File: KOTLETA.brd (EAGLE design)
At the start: 27 x 40.2 mm, 107 parts, among them CON1 SM06B-SRSS-TB, CON2 CON-4P-JST_GH-RA, CON3 CON-4P-JST_GH-RA, IC1 STM32F105RCT6, IC2 CAT24C02, IC3 SN65HVD232D, IC4 LMR14010ADDCT, IC5 LM75BD-TSSOP8, IC6 FAN7888, IC7 ZXCT1051, IC8 3.3V, Q1 CSD18510Q5B, Q2 CSD18510Q5B, Q3 CSD18510Q5B, Q4 CSD18510Q5B, Q5 CSD18510Q5B, Q6 CSD18510Q5B, X1 24MHz

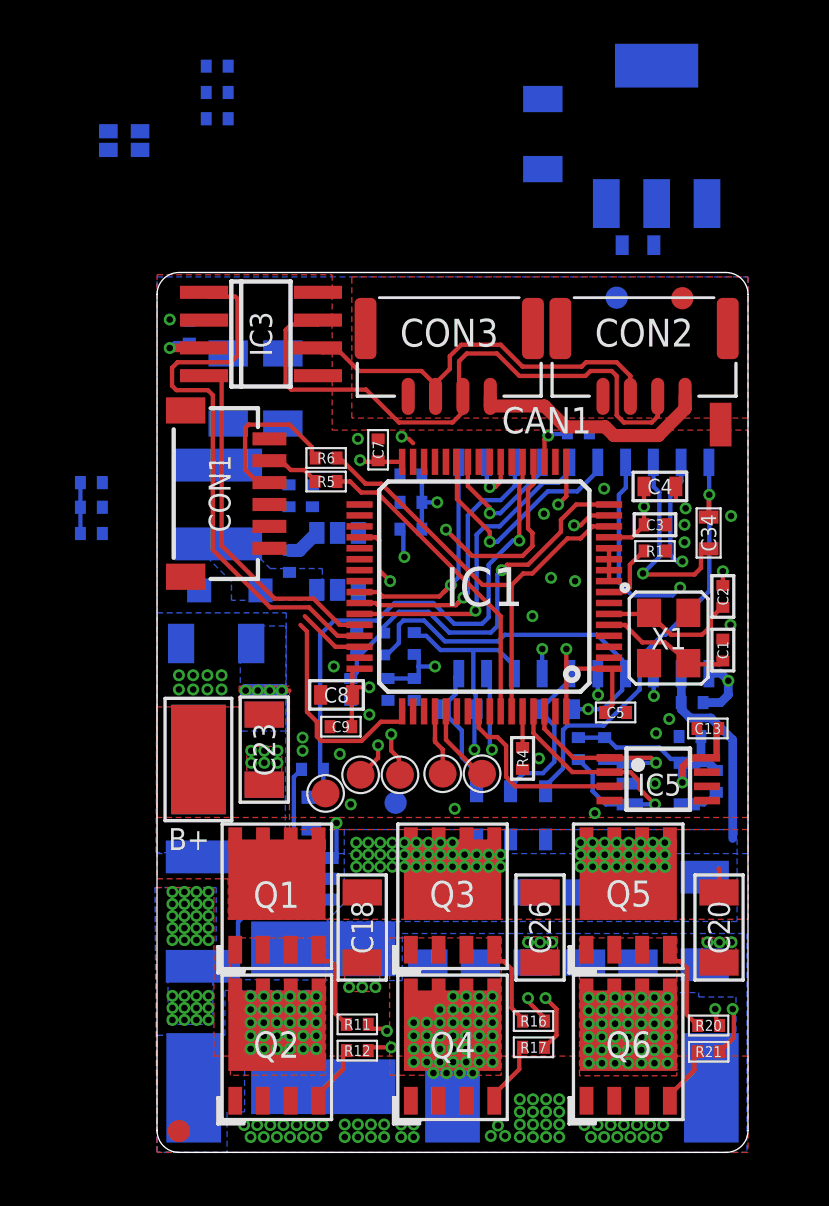
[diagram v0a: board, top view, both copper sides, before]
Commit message: proper gitignore
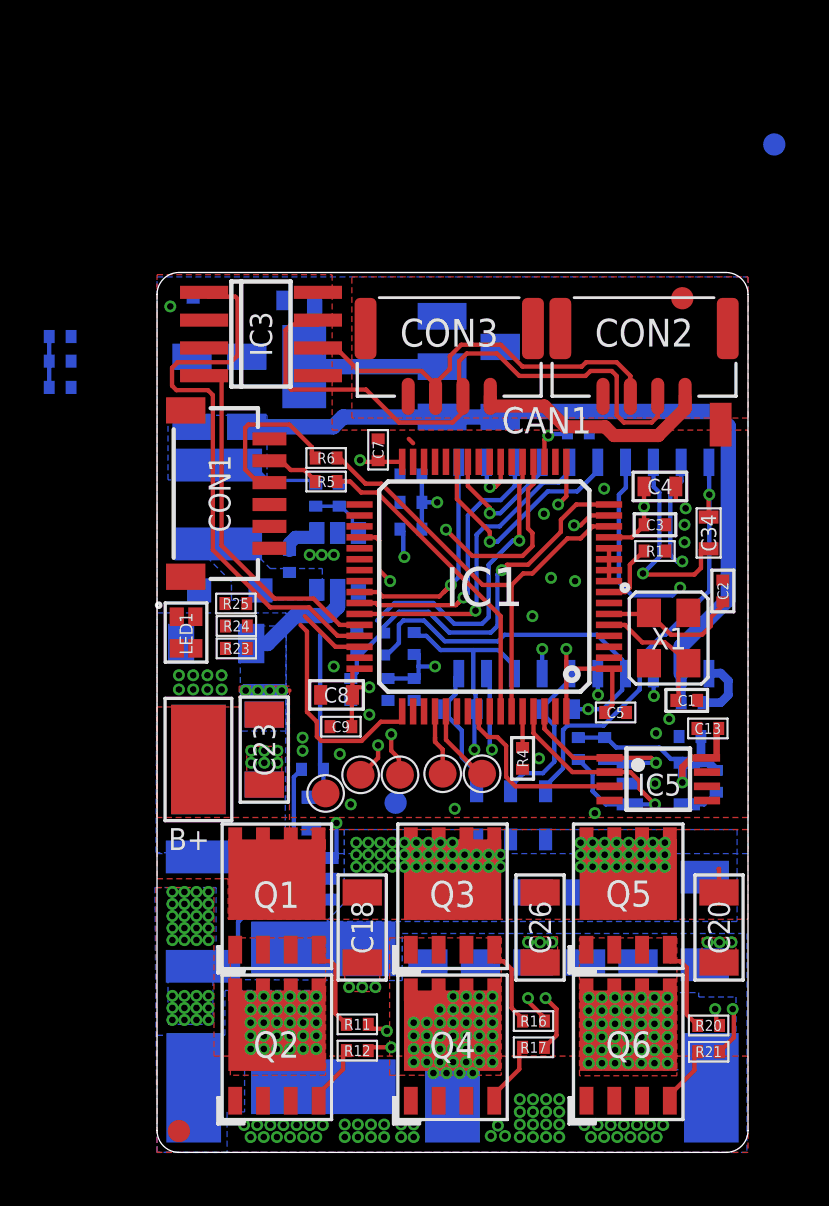
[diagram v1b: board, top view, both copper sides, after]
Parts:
- moved R25 24.6 mm to (3.60, 25.1), flipped to the top
- moved R24 24.4 mm to (3.62, 24.1), flipped to the top
- moved R23 24.2 mm to (3.62, 23.0), flipped to the top
- moved LED1 22.7 mm to (1.32, 23.8), flipped to the top, turned to 0 degrees
- moved IC8 16.7 mm to (9.88, 35.9), turned to 270 degrees
- moved C29 15.7 mm to (6.47, 38.9)
- moved C27 11.5 mm to (15.7, 35.2)
- moved FD3 10.0 mm to (28.2, 46.0)
- moved R9 6.83 mm to (-4.42, 35.0)
- moved C15 6.83 mm to (-4.42, 37.3)
- moved R8 6.83 mm to (-4.42, 36.1)
- moved C1 2.83 mm to (24.2, 20.6), turned to 180 degrees
- moved C36 1.66 mm to (4.10, 34.8)
- moved C38 1.66 mm to (1.60, 34.8)
- moved R27 1.23 mm to (7.25, 30.0)
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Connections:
- net VBAT: no longer C14.1, IC6.12
- net VDD_9V: now also C14.1, IC6.12
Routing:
- net VDD_9V: track 0.72 -> 40.9 mm
- net VDD_3V3: track 40.4 -> 47.4 mm, vias 9 -> 8
- net VBAT: track 14.4 -> 10.7 mm
- net SENSE_CURRENT: track 24.7 -> 21.8 mm
- net N$24: track 0.00 -> 2.71 mm
- net GND: track 8.41 -> 7.76 mm, vias 41 -> 38
- net N$7: track 0.64 -> 0.00 mm
- added copper zone on layer 16, net VDD_9V

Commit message: routing done
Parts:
- R14: value 0.005 OHM -> 0.005R; device sapog_reference_hardware:2010_CURRENT_SHUNT -> SHUNT_RESISTORS:R2010-KELVIN
- X1: device GNSS2_master_lib:OSCILLATOR-3.2X2.5 -> crystal:OSCILLATOR-3.2X2.5-4P
- moved C28 19.4 mm to (15.7, 32.9), flipped to the top, turned to 0 degrees
- moved C15 16.3 mm to (10.2, 30.1), turned to 90 degrees
- moved R9 14.5 mm to (9.22, 30.1), turned to 270 degrees
- moved R8 13.9 mm to (8.72, 31.6), turned to 0 degrees
- moved R7 9.10 mm to (11.8, 25.3)
- moved FD3 7.32 mm to (25.6, 39.2)
- moved C29 2.52 mm to (4.15, 38.0)
- moved C9 1.80 mm to (8.40, 21.2)
- moved C7 1.39 mm to (11.2, 33.0), turned to 180 degrees
- moved C8 1.30 mm to (8.80, 19.8)
- moved C30 1.06 mm to (9.90, 21.3)
- moved TP3 0.89 mm to (7.42, 17.2)
- moved R18 0.78 mm to (11.1, 23.2), turned to 270 degrees
- moved CON2 0.70 mm to (22.2, 38.1)
- moved CON3 0.70 mm to (13.3, 38.1)
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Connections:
- removed net N$15: IC7.4, R14.SENSE1
- new net N$20: IC7.4, R14.S1
- net CURRENT_SHUNT: now also R14.1, R14.11; no longer R14.CURRENT1
- net GND: now also R14.2, R14.22; no longer R14.CURRENT2
- net GNDD: no longer IC3.5
- net N$13: now also R14.S2; no longer R14.SENSE2
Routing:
- net N$12: track 0.00 -> 13.6 mm, vias 0 -> 2
- net SWDIO: track 3.08 -> 16.4 mm, vias 0 -> 2
- net SWCLK: track 10.2 -> 22.8 mm, vias 0 -> 2
- net BLABLA: track 7.08 -> 17.5 mm
- net N$3: track 0.00 -> 10.2 mm, vias 0 -> 2
- net N$18: track 0.00 -> 9.53 mm, vias 0 -> 2
- net SENSE_CURRENT: track 21.8 -> 12.7 mm
- net GNDD: track 0.59 -> 7.85 mm, vias 0 -> 2
- net VDD_3V3: track 47.4 -> 54.0 mm, vias 8 -> 15
- net SENSE_VIN: track 11.0 -> 16.1 mm
- net N$20: track 0.00 -> 5.04 mm
- net VDD_9V: track 40.9 -> 44.7 mm
- net VBAT: track 10.7 -> 14.5 mm
- net N$15: track 3.20 -> 0.00 mm
- net N$25: track 19.5 -> 22.4 mm
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- added copper zone on layer 16, net VDD_3V3
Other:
- board text removed: "CAN1"

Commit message: updates
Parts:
- CON1: value SM06B-SRSS-TB -> CON-6P; device sapog_reference_hardware:SM06B -> Connectors:SM06B
- IC2: device sapog_reference_hardware:SOT23-5L -> misc:SOT23-5L
- IC5: device sapog_reference_hardware:TSSOP8 -> misc:TSSOP8
- IC8: device sapog_reference_hardware:SOT-223 -> linear regulators:SOT-223
- LED1: device sapog_reference_hardware:LITE_ON_RGB_LED -> myxa_masterlib:LITE_ON_RGB_LED
- moved R2 0.12 mm to (20.3, 18.4)

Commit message: Updates
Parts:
- removed R28: (no value), rc:R0402
- removed U$1: (no value), sapog_reference_hardware:REF_BOARD_OUTLINE
- added PAD1, PAD10, PAD11, PAD12, PAD13, PAD14, PAD15, PAD16, PAD17, PAD18, PAD19, PAD2, PAD3, PAD4, PAD5, PAD6, PAD7, PAD8, PAD9: PAD-HOLE-0.6, PADS:HOLE_0.6
- added R29: 200R, R_digikey:R0402
- added R30: 10K, R_digikey:R0402
- R27: value (none) -> 130K
- moved FD2 24.8 mm to (25.8, 2.05)
- moved FD1 12.0 mm to (11.7, 39.1)
- moved FD3 1.10 mm to (25.7, 38.1)
- moved B+ 0.08 mm to (1.97, 17.9)
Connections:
- new net N$15: IC1.9, R29.1
- net FET_A_VS: now also PAD17.P$1, PAD7.P$1, PAD8.P$1
- net FET_B_VS: now also PAD10.P$1, PAD18.P$1, PAD9.P$1
- net FET_C_VS: now also PAD11.P$1, PAD12.P$1, PAD19.P$1
- net GND: now also PAD4.P$1, PAD5.P$1, PAD6.P$1, R30.1; no longer IC1.9, R28.1
- net GNDD: now also PAD13.P$1
- net N$22: now also PAD16.P$1
- net N$23: now also PAD15.P$1
- net N$24: now also R30.2; no longer R28.2
- net N$25: now also PAD14.P$1
- net VBAT: now also PAD1.P$1, PAD2.P$1, PAD3.P$1
- net VDD_3V3: now also R29.2
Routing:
- net N$15: track 0.00 -> 8.87 mm, vias 0 -> 1
- net N$22: track 11.1 -> 16.4 mm
- net N$23: track 27.7 -> 33.0 mm
- net GNDD: track 7.85 -> 3.25 mm, vias 2 -> 3
- net N$25: track 22.4 -> 26.4 mm
- net VDD_3V3: track 54.0 -> 57.6 mm
- net FET_A_VS: track 24.8 -> 27.9 mm
- net FET_B_VS: track 29.3 -> 32.3 mm
- net FET_C_VS: track 42.5 -> 45.1 mm
- net VDD_9V: track 44.7 -> 44.1 mm
- net GND: track 8.74 -> 8.24 mm, vias 59 -> 57
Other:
- outline, holes or cut-outs redrawn

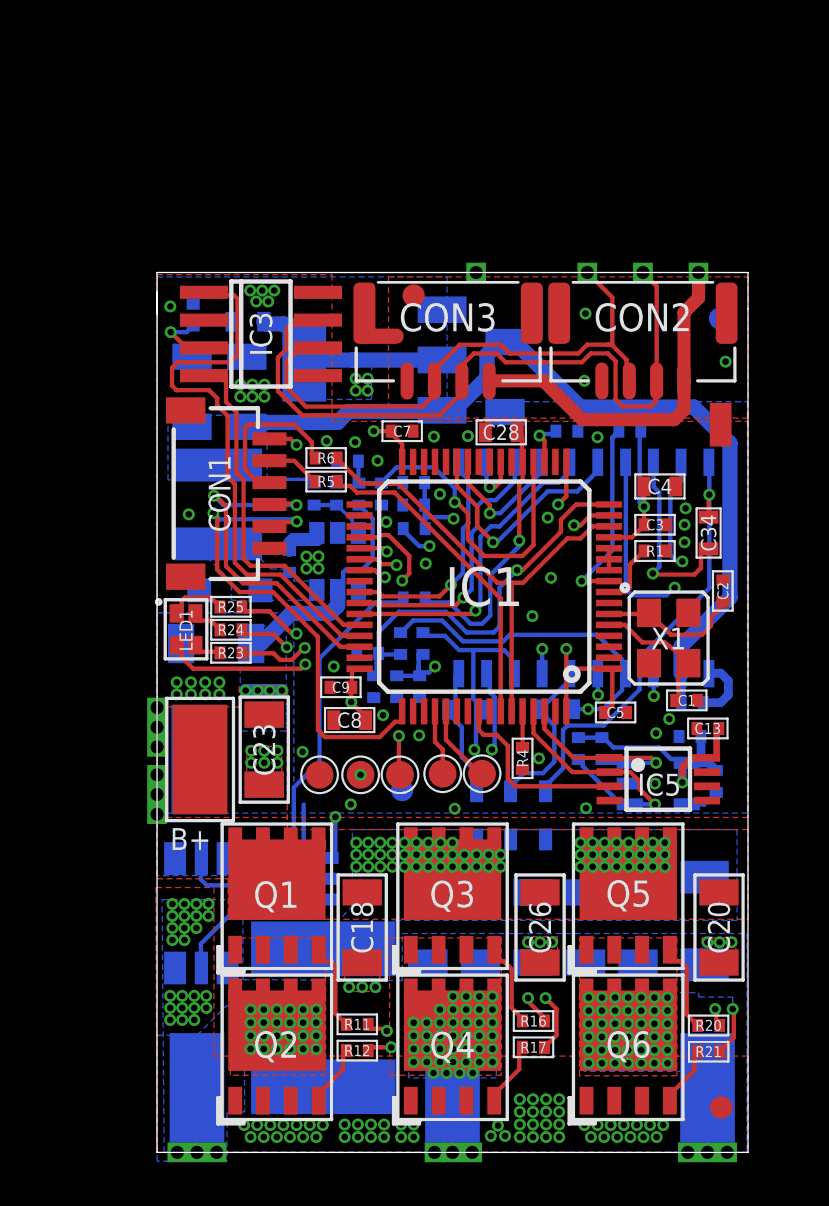
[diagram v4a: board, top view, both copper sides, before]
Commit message: BETTER polygons
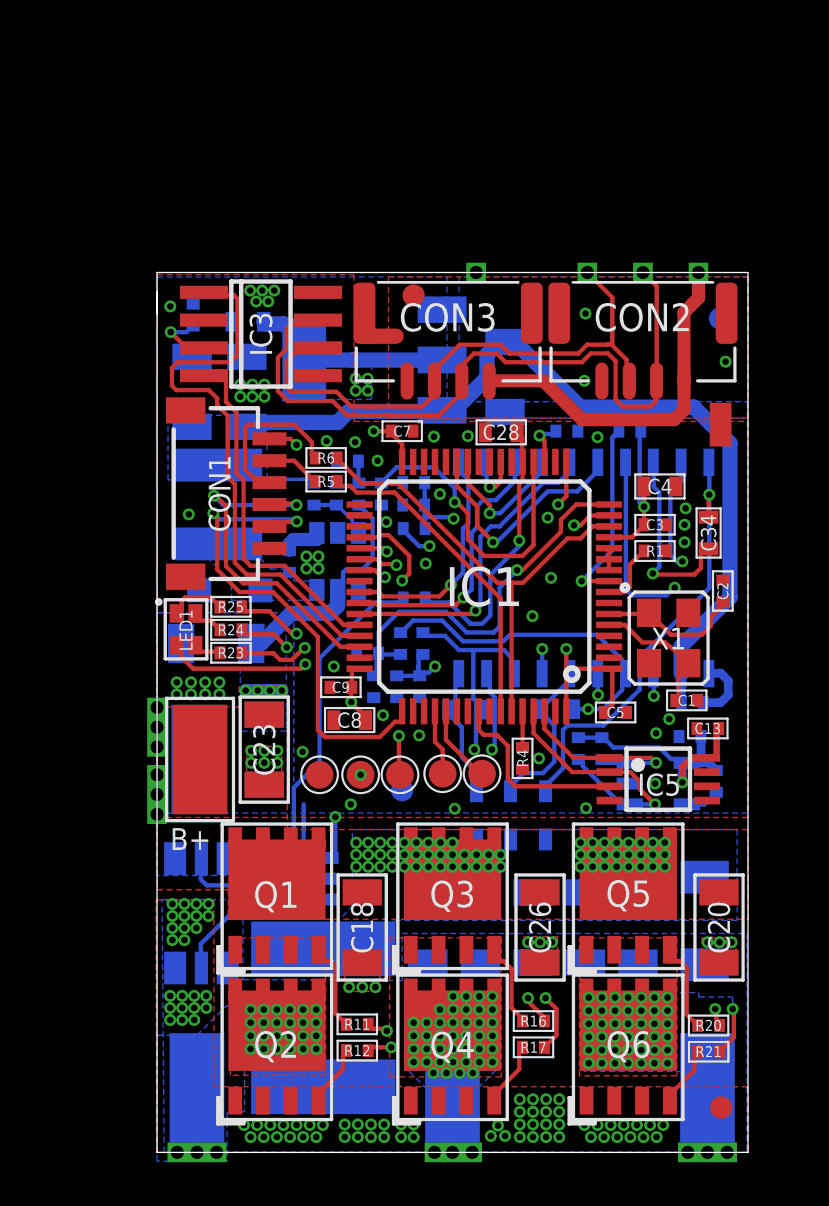
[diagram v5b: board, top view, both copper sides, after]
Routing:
- added copper zone on layer 16, net GNDD
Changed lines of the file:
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@@
 <grid distance="0.025" unitdist="mm" unit="mm" style="lines" multiple="2" display="no" altdistance="1" altunitdist="mm" altunit="mm"/>
 <layers>
-<layer number="1" name="Top" color="4" fill="1" visible="no" active="yes"/>
+<layer number="1" name="Top" color="4" fill="1" visible="yes" active="yes"/>
 <layer number="2" name="gnd" color="1" fill="3" visible="no" active="yes"/>
 <layer number="3" name="SUPPLY" color="2" fill="5" visible="no" active="yes"/>
@@
 <layer number="14" name="Horizontal" color="13" fill="1" visible="no" active="no"/>
 <layer number="15" name="+3v3" color="4" fill="6" visible="no" active="no"/>
-<layer number="16" name="Bottom" color="1" fill="1" visible="yes" active="yes"/>
+<layer number="16" name="Bottom" color="1" fill="1" visible="no" active="yes"/>
 <layer number="17" name="Pads" color="2" fill="1" visible="yes" active="yes"/>
 <layer number="18" name="Vias" color="2" fill="1" visible="yes" active="yes"/>
 <layer number="19" name="Unrouted" color="14" fill="1" visible="yes" active="yes"/>
 <layer number="20" name="Dimension" color="15" fill="1" visible="yes" active="yes"/>
-<layer number="21" name="tPlace" color="7" fill="1" visible="no" active="yes"/>
-<layer number="22" name="bPlace" color="7" fill="1" visible="yes" active="yes"/>
-<layer number="23" name="tOrigins" color="15" fill="1" visible="no" active="yes"/>
-<layer number="24" name="bOrigins" color="15" fill="1" visible="yes" active="yes"/>
-<layer number="25" name="tNames" color="7" fill="1" visible="no" active="yes"/>
-<layer number="26" name="bNames" color="7" fill="1" visible="yes" active="yes"/>
+<layer number="21" name="tPlace" color="7" fill="1" visible="yes" active="yes"/>
+<layer number="22" name="bPlace" color="7" fill="1" visible="no" active="yes"/>
+<layer number="23" name="tOrigins" color="15" fill="1" visible="yes" active="yes"/>
+<layer number="24" name="bOrigins" color="15" fill="1" visible="no" active="yes"/>
+<layer number="25" name="tNames" color="7" fill="1" visible="yes" active="yes"/>
+<layer number="26" name="bNames" color="7" fill="1" visible="no" active="yes"/>
 <layer number="27" name="tValues" color="7" fill="1" visible="no" active="yes"/>
 <layer number="28" name="bValues" color="7" fill="1" visible="no" active="yes"/>
@@
 <layer number="49" name="Reference" color="7" fill="1" visible="no" active="yes"/>
 <layer number="50" name="dxf" color="7" fill="1" visible="no" active="no"/>
-<layer number="51" name="tDocu" color="7" fill="1" visible="no" active="yes"/>
-<layer number="52" name="bDocu" color="7" fill="1" visible="yes" active="yes"/>
+<layer number="51" name="tDocu" color="7" fill="1" visible="yes" active="yes"/>
+<layer number="52" name="bDocu" color="7" fill="1" visible="no" active="yes"/>
 <layer number="53" name="tGND_GNDA" color="7" fill="9" visible="no" active="no"/>
 <layer number="54" name="bGND_GNDA" color="1" fill="9" visible="no" active="no"/>
@@
 </layers>
 <board>
-<fusionsync huburn="a.cGVyc29uYWw6dWUyYWE4ZDY4" projecturn="a.cGVyc29uYWw6dWUyYWE4ZDY4IzIwMTkwMjAzMTc0MDAzODgx" f3durn="urn:adsk.wipprod:dm.lineage:CTH-7dBBS_G654204HbCxw" pcbguid="6951ede2-7dc7-4c16-80e3-2d825fdd5a87" lastpulledtime="" lastsyncedchangeguid="1851f7f4-73dc-d163-4d93-8e47587d1237"/>
+<fusionsync huburn="a.cGVyc29uYWw6dWUyYWE4ZDY4" projecturn="a.cGVyc29uYWw6dWUyYWE4ZDY4IzIwMTkwMjAzMTc0MDAzODgx" f3durn="urn:adsk.wipprod:dm.lineage:CTH-7dBBS_G654204HbCxw" pcbguid="6951ede2-7dc7-4c16-80e3-2d825fdd5a87" lastpulledtime="" lastsyncedchangeguid="34d018ec-711d-4d17-0580-f986b27920b4"/>
 <plain>
 <dimension x1="0" y1="0" x2="1.9" y2="17.95" x3="-3.65" y3="8.975" textsize="1" layer="47" dtype="vertical" width="0.1"/>
@@
 <vertex x="3.75" y="20.35"/>
 <vertex x="0" y="20.35"/>
-<vertex x="0" y="12.5"/>
-<vertex x="3.25" y="12.5"/>
+<vertex x="0" y="12"/>
+<vertex x="3.25" y="12"/>
 <vertex x="3.25" y="10.65"/>
 <vertex x="27" y="10.65"/>
@@
 <vertex x="0" y="15.3"/>
 <vertex x="0" y="40.1"/>
-<vertex x="8" y="40.1"/>
-<vertex x="8" y="33.4"/>
+<vertex x="9" y="40.1"/>
+<vertex x="9" y="33.4"/>
 <vertex x="27" y="33.4"/>
 <vertex x="27" y="15.3"/>
@@
 <vertex x="10.625" y="9.8"/>
 <vertex x="15.725" y="9.8"/>
-<vertex x="15.725" y="3.525"/>
-<vertex x="10.625" y="3.525"/>
+<vertex x="15.725" y="3.45"/>
+<vertex x="10.625" y="3.45"/>
 </polygon>
 <via x="13.525" y="7.125" extent="1-16" drill="0.3"/>
@@
 <via x="11.725" y="4.125" extent="1-16" drill="0.3"/>
 <via x="15.325" y="4.125" extent="1-16" drill="0.3"/>
-<polygon width="0.2" layer="16" thermals="no">
-<vertex x="11.5" y="6.125"/>
-<vertex x="12.625" y="6.125"/>
-<vertex x="12.625" y="6.575"/>
-<vertex x="13.45" y="7.35"/>
-<vertex x="15.5" y="7.35"/>
-<vertex x="15.5" y="3.4"/>
-<vertex x="11.5" y="3.4"/>
-</polygon>
 <wire x1="14.135" y1="7.44" x2="14.125" y2="7.43" width="0.2" layer="1"/>
 <wire x1="14.125" y1="7.43" x2="14.125" y2="7.125" width="0.2" layer="1"/>
@@
 <contactref element="PAD18" pad="P$1"/>
 <wire x1="13.5" y1="2.95" x2="13.5" y2="0" width="0.2" layer="16"/>
-<wire x1="13.5" y1="0" x2="14.4" y2="0" width="0" layer="19" extent="1-1"/>
-<wire x1="12.675" y1="0" x2="13.5" y2="0" width="0" layer="19" extent="1-1"/>
+<polygon width="0.1524" layer="16" thermals="no">
+<vertex x="12.325" y="-0.325"/>
+<vertex x="14.675" y="-0.325"/>
+<vertex x="14.675" y="2.95"/>
+<vertex x="15.525" y="3.8"/>
+<vertex x="15.525" y="7.325"/>
+<vertex x="12.8" y="7.325"/>
+<vertex x="11.525" y="6.05"/>
+<vertex x="11.525" y="3.7"/>
+<vertex x="12.325" y="2.9"/>
+</polygon>
 </signal>
 <signal name="FET_C_HO">
@@
 <wire x1="6.125" y1="37.825" x2="7.35" y2="37.825" width="0.2" layer="1"/>
 <wire x1="7.35" y1="37.825" x2="7.35" y2="38.025" width="0.2" layer="1"/>
-<wire x1="5.525" y1="34.7843125" x2="5.525" y2="36.3156875" width="0.2" layer="1"/>
+<wire x1="5.525" y1="36.3156875" x2="5.525" y2="34.7843125" width="0.2" layer="1"/>
 <wire x1="5.525" y1="36.3156875" x2="5.925" y2="36.7156875" width="0.2" layer="1"/>
 <wire x1="5.925" y1="37.625" x2="6.125" y2="37.825" width="0.2" layer="1"/>
 <wire x1="5.925" y1="36.7156875" x2="5.925" y2="37.625" width="0.2" layer="1"/>
-<wire x1="6.6343125" y1="33.675" x2="12.9" y2="33.675" width="0.2" layer="1"/>
-<wire x1="6.6343125" y1="33.675" x2="5.525" y2="34.7843125" width="0.2" layer="1"/>
+<wire x1="8.675" y1="33.675" x2="12.9" y2="33.675" width="0.2" layer="1"/>
 <wire x1="19.82034375" y1="36.50465625" x2="19.4156875" y2="36.1" width="0.2" layer="1"/>
 <wire x1="19.82034375" y1="36.50465625" x2="20.59534375" y2="36.50465625" width="0.2" layer="1"/>
@@
 <wire x1="22.825" y1="35.24" x2="22.825" y2="39.575" width="0.2" layer="1"/>
 <wire x1="22.825" y1="39.575" x2="22.2" y2="40.2" width="0.2" layer="1"/>
+<wire x1="5.525" y1="34.7843125" x2="5.9843125" y2="34.325" width="0.2" layer="1"/>
+<wire x1="8.025" y1="34.325" x2="8.675" y2="33.675" width="0.2" layer="1"/>
+<wire x1="5.9843125" y1="34.325" x2="8.025" y2="34.325" width="0.2" layer="1"/>
 </signal>
 <signal name="N$25">
@@
 <wire x1="5.925" y1="36.15" x2="5.925" y2="34.95" width="0.2" layer="1"/>
 <wire x1="6.4525" y1="36.6775" x2="7.4275" y2="36.6775" width="0.2" layer="1"/>
-<wire x1="12.125" y1="34.075" x2="6.8" y2="34.075" width="0.2" layer="1"/>
+<wire x1="12.125" y1="34.075" x2="9.875" y2="34.075" width="0.2" layer="1"/>
 <wire x1="5.925" y1="36.15" x2="6.4525" y2="36.6775" width="0.2" layer="1"/>
-<wire x1="5.925" y1="34.95" x2="6.8" y2="34.075" width="0.2" layer="1"/>
 <wire x1="19.25" y1="36.5" x2="19.65465625" y2="36.90465625" width="0.2" layer="1"/>
 <wire x1="20.76103125" y1="36.90465625" x2="21.45" y2="36.2156875" width="0.2" layer="1"/>
@@
 <wire x1="20.8" y1="36.90465625" x2="20.8" y2="39.06" width="0.2" layer="1"/>
 <wire x1="20.8" y1="39.06" x2="19.66" y2="40.2" width="0.2" layer="1"/>
+<wire x1="5.925" y1="34.95" x2="6.125" y2="34.75" width="0.2" layer="1"/>
+<wire x1="6.125" y1="34.75" x2="8.2" y2="34.75" width="0.2" layer="1"/>
+<wire x1="8.2" y1="34.75" x2="8.875" y2="34.075" width="0.2" layer="1"/>
+<wire x1="8.875" y1="34.075" x2="9.875" y2="34.075" width="0.2" layer="1"/>
 </signal>
 <signal name="BOOT0">
@@
 <polygon width="0.2" layer="1" thermals="no" rank="3">
 <vertex x="0" y="0"/>
-<vertex x="-0.05" y="12.1"/>
-<vertex x="2.6" y="12.1"/>
-<vertex x="2.6" y="4.4"/>
-<vertex x="27" y="4.4"/>
+<vertex x="-0.047625" y="11.525"/>
+<vertex x="2.6" y="11.525"/>
+<vertex x="2.6" y="3"/>
+<vertex x="27" y="3"/>
 <vertex x="27" y="0"/>
 </polygon>
@@
 <contactref element="PAD13" pad="P$1"/>
 <via x="25.975" y="36.125" extent="1-16" drill="0.3" diameter="0.55"/>
+<polygon width="0.2" layer="16" rank="4">
+<vertex x="27" y="40"/>
+<vertex x="13.8" y="40"/>
+<vertex x="13.8" y="33.55"/>
+<vertex x="27" y="33.55"/>
+</polygon>
 </signal>
 <signal name="N$27">

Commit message: minor fixes
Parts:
- moved C2 2.50 mm to (25.9, 23.1), turned to 90 degrees
- moved FD1 0.90 mm to (12.6, 39.4)
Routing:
- net GNDD: track 3.25 -> 8.02 mm
- net GND: track 8.24 -> 5.27 mm, vias 57 -> 63
- net N$21: track 6.58 -> 5.93 mm

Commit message: BOM fixes
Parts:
- R14: value 0.005R -> 0.001R
